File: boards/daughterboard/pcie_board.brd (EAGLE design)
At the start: 97.3 x 93 mm, 61 parts, among them IC1 XMEGA16A4A, IC2 SN754410, T1 2N3704, T2 2N3704, T3 2N3704, T4 2N3704, T5 2N3704, T6 2N3704, T7 2N3704, X1 PCI-E1X_EDGE

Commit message: Latest board(the one presented at class
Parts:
- removed ANALOG_IN, JTAG: (no value), pinhead:2X03
- removed ASYNC_INT_IN: (no value), pinhead:2X02
- removed C1, C2: (no value), capacitor-wima:C2.5-4
- removed LED_ERROR, LED_MOT_A, LED_MOT_B, LED_SELECTED: (no value), led:LED5MM
- removed MOT_A_OUT, MOT_B_OUT, TRIAC_OUT, ZEROCROSS_SENSE: (no value), pinhead:1X02
- removed PWR, PWR1, PWR2: (no value), pinhead:1X04
- removed S1: (no value), switch-dil:DA-05
- removed T1, T2, T3, T4, T5, T6, T7: 2N3704, transistor:TO92
- added CHANNEL_1_ADC, CHANNEL_2_ADC, I2C1, I2C2, JP4, JP5, JP6, OPTO_IN: (no value), pinhead:1X02
- added JP1, JP3: (no value), pinhead:2X03
- added JP10, JP11, JP12, JP13, MOTOR_1_OUT, MOTOR_2_OUT: (no value), SparkFun:SCREWTERMINAL-3.5MM-2
- added JP2, JP7, JP8, JP9, SLAVE_SELECT_2: (no value), pinhead:1X01
- added LED1, LED2, LED3: (no value), led:CHIP-LED0603
- added LED_ERROR1, LED_ERROR2, LED_MOT1, LED_MOT2: (no value), led:LED5MM
- added MPC3002ADC: (no value), ic-package:DIL08
- added OK3: TIL193, optocoupler:DIL16
- added R29, R30, R31, R32: (no value), resistor:M0805
- added SPI_OUT: (no value), pinhead:1X05
- added U$1: PCI-E1X_EDGE, con-pci_express(pci-e):PCI-E_X1_EDGE
- EXTERNAL_POWER_IN: device pinhead:1X02 -> SparkFun:SCREWTERMINAL-3.5MM-2
- OK1, OK2: value ILQ620 -> TIL193
- R1, R2, R22, R3, R5, R6, R7: value 10K -> (none); device resistor:R0805 -> resistor:M0805
- R10, R11, R15, R16, R17, R8, R9: value 47Ohm -> (none); device resistor:0207/10 -> resistor:M0805
- R12, R4: value 100Ohm -> (none); device resistor:0207/10 -> resistor:M0805
- R13, R14, R18, R19, R20: value 100Ohm -> (none); device resistor:R0805 -> resistor:M0805
- R21: value 10K -> (none); device resistor:0207/10 -> resistor:M0805
- R23, R24, R25, R26, R27, R28: value 47Ohm -> (none); device resistor:0204/7 -> resistor:M0805
- X1: value PCI-E1X_EDGE -> 9090-4R; device con-pci_express(pci-e):PCI-E_X1_EDGE -> con-thomas-betts:9090-4R
- moved R23 79.8 mm to (66.3, 23.4), turned to 0 degrees
- moved R28 79.0 mm to (72.6, -1.02)
- moved R24 71.5 mm to (66.3, 28.4), turned to 0 degrees
- moved R18 71.1 mm to (9.65, 11.9), flipped to the top
- moved R26 69.5 mm to (72.9, 31.2)
- moved R15 64.7 mm to (9.65, 33.0), turned to 0 degrees
- moved R17 64.3 mm to (9.65, 19.6), turned to 0 degrees
- moved R16 62.4 mm to (9.65, 27.2), turned to 0 degrees
- moved R1 53.7 mm to (28.7, 48.8)
- moved X1 52.4 mm to (12.7, 61.7)
- moved R3 51.3 mm to (28.7, 43.4), turned to 0 degrees
- moved R2 48.8 mm to (28.7, 53.8), turned to 0 degrees
- moved R8 48.7 mm to (49.5, -2.54), turned to 0 degrees
- moved R25 47.1 mm to (54.1, 51.6), turned to 90 degrees
- moved R4 45.3 mm to (53.6, -2.54), flipped to the top, turned to 180 degrees
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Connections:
- removed net +12V: PWR.1, PWR1.1, PWR2.1, X1.A3, X1.B3
- removed net +5V: PWR.2, PWR1.2, PWR2.2, X1.A2, X1.B2
- removed net EXT_5V: IC2.16, R1.2, R2.1, R22.2, R3.1, R5.2, R6.1, R7.1, VREG.OUT
- removed net N$15: IC1.13, R27.1
- removed net N$4: LED_POWER.A, R23.2
- removed net N$43: IC2.14, MOT_B_OUT.1
- removed net N$45: IC1.16, S1.7
- removed net N$46: IC1.15, S1.6
- removed net N$47: OK2.3, R10.1
- removed net N$48: OK2.5, R11.1
- removed net N$49: OK2.4, T2.2
- removed net N$50: OK2.6, T3.2
- removed net N$51: R12.1, T1.1
- removed net N$52: R13.1, T2.1
- removed net N$53: R14.1, T3.1
- removed net N$55: IC1.23, R14.2
- removed net N$56: IC1.24, R13.2
- removed net N$57: OK1.2, T4.2
- removed net N$58: OK1.4, T5.2
- removed net N$59: OK1.6, T6.2
- removed net N$60: R18.1, T4.1
- removed net N$61: R19.1, T5.1
- removed net N$62: R20.1, T6.1
- removed net N$65: IC1.25, R19.2
- removed net N$66: IC1.26, R20.2
- removed net N$67: OK1.1, R15.1
- removed net N$68: OK1.3, R16.1
- removed net N$69: OK1.5, R17.1
- removed net N$70: IC1.44, S1.8
- removed net N$71: ANALOG_IN.2, IC1.4
- removed net N$73: ANALOG_IN.5, IC1.40
- removed net N$74: ANALOG_IN.3, IC1.41
- removed net N$75: ASYNC_INT_IN.1, IC1.42
- removed net N$77: IC1.1, R23.1
- removed net PWM_A: IC1.21, R12.2
- removed net TRIAC_OUT: IC1.17, R4.2
- removed net ZEROCROSS_IN: IC1.27, OK2.10, R21.1
- new net ADC_CLK: MPC3002ADC.7, OK3.16, R30.1, SPI_OUT.3
- new net ADC_CS: MPC3002ADC.1, OK1.10, R27.1
- new net ADC_MISO: MPC3002ADC.6, R28.1, SPI_OUT.2
- new net ADC_MOSI: MPC3002ADC.5, OK3.14, R29.1, SPI_OUT.1
- new net ADC_VSS: CHANNEL_2_ADC.1, IC2.16, LED3.A, R19.2, R20.2, R21.1, R22.2, R23.2, R24.2, R27.2, R29.2, R30.2, R31.2, SPI_OUT.5, VREG.OUT
- new net ANALOG_1: IC1.40, JP1.1
- new net ANALOG_2: IC1.41, JP1.2
- new net ANALOG_3: IC1.43, JP1.3
- new net ANALOG_4: IC1.44, JP1.4
- new net ANALOG_5: IC1.1, JP1.5
- new net ANALOG_6: IC1.2, JP1.6
- new net ASYNC_1: IC1.22, JP8.1
- new net ASYNC_2: IC1.12, JP2.1
- new net ASYNC_3: IC1.6, JP9.1
- new net ASYNC_4: IC1.42, JP7.1
- new net CHANNEL_1: CHANNEL_1_ADC.1, MPC3002ADC.2
- new net LED_ERROR1: IC1.25, R15.2
- new net LED_ERROR2: IC1.26, R16.2
- new net LED_MOT_1: IC1.27, R17.2
- new net LED_MOT_2: IC1.33, R18.2
- new net LED_ORDERS: IC1.24, R14.2
- new net LED_POWER: IC1.23, R13.2
- new net MISO: IC1.16, OK3.12, R4.1
- new net MOSI: IC1.15, OK3.3
- new net MOT_CONTROL_A_1: IC1.13, OK1.3
- new net MOT_CONTROL_A_2: IC1.7, OK2.3
- new net MOT_CONTROL_B_1: IC1.14, OK1.5
- new net MOT_CONTROL_B_2: IC1.5, OK2.5
- new net MOT_CONTROL_EN_1: IC1.21, OK1.1
- new net MOT_CONTROL_EN_2: IC1.20, OK2.1
- new net N$38: JP10.1, JP11.1, X1.1
- new net OPTIONAL_OPTO_IN: OK3.10, R8.1
- new net PDI_CLK: IC1.35, JP3.2
- new net PDI_DATA: IC1.34, JP3.6
- new net SCK: IC1.17, OK3.1
- new net SS1: IC1.3, OK2.7
- new net SS2: IC1.4, OK1.7
- net +3V3: now also JP3.5, JP4.1, JP5.1, JP6.1, R4.2, U$1.A1, U$1.A2, U$1.B1, U$1.B2; no longer C1.1, C2.2, JTAG.2, PWR.3, PWR1.3, PWR2.3, R10.2, R11.2, R15.2, R16.2, R17.2, R21.2, R9.2, S1.1, S1.2, S1.3, S1.4, S1.5, X1.A1, X1.B1
- net ERROR: now also IC1.32, U$1.A7, U$1.B7; no longer IC1.22, X1.A6
- net EXT_MOTOR_GND: now also CHANNEL_2_ADC.2, MPC3002ADC.4, MPC3002ADC.8, OK2.9, OK3.13, OK3.15, OK3.6, R25.2, R26.2, R32.2, SPI_OUT.4; no longer TRIAC_OUT.2
- net GND: now also JP10.2, JP11.2, JP12.2, JP13.2, JP3.1, JP4.2, JP5.2, LED_ERROR1.K, LED_ERROR2.K, LED_MOT1.K, LED_MOT2.K, OK3.11, OK3.9, R1.1, R10.1, R11.1, R12.1, R2.1, R3.1, R5.1, R6.1, R7.1, R9.1, U$1.A10, U$1.A11, U$1.A12, U$1.A13, U$1.A14, U$1.A15, U$1.A16, U$1.A17, U$1.A18, U$1.A8, U$1.A9, U$1.B10, U$1.B11, U$1.B12, U$1.B13, U$1.B14, U$1.B15, U$1.B16, U$1.B17, U$1.B18, U$1.B8, U$1.B9, X1.2, X1.3; no longer C1.2, C2.1, JTAG.6, LED_ERROR.K, LED_MOT_A.K, LED_MOT_B.K, LED_SELECTED.K, OK2.9, PWR.4, PWR1.4, PWR2.4, T1.3, T2.3, T3.3, T4.3, T5.3, T6.3, T7.3, X1.A10, X1.A12, X1.A13, X1.A14, X1.A15, X1.A16, X1.A17, X1.A18, X1.A4, X1.A5, X1.A7, X1.A8, X1.B10, X1.B11, X1.B12, X1.B13, X1.B14, X1.B15, X1.B16, X1.B17, X1.B18, X1.B4, X1.B5, X1.B7, X1.B9
- net N$1: now also IC2.14, MOTOR_2_OUT.1; no longer IC1.3, R25.1
- net N$10: now also OK2.4, R6.2; no longer IC1.33, R26.1
- net N$11: now also OK2.6, R7.2; no longer LED_ERROR.A, R26.2
- net N$12: now also OK2.8, R10.2; no longer ANALOG_IN.4, IC1.5
- net N$13: now also OK3.2, R11.2; no longer ANALOG_IN.6, IC1.7
- net N$14: now also OK3.4, R12.2; no longer ASYNC_INT_IN.3, IC1.12
- net N$16: now also LED_POWER.A, R13.1; no longer ANALOG_IN.1, IC1.43
- net N$17: now also LED_ORDERS.A, R14.1; no longer IC1.14, R28.1
- net N$18: now also CHANNEL_1_ADC.2, MPC3002ADC.3; no longer ASYNC_INT_IN.4, IC1.32
- net N$19: now also OK2.10, R31.1, SLAVE_SELECT_2.1; no longer LED_MOT_B.A, R28.2
- net N$2: now also JP12.1, JP13.1, X1.4; no longer IC1.35, JTAG.5
- net N$20: now also LED_ERROR1.A, R15.1; no longer IC1.2, R24.1
- net N$21: now also LED_ERROR2.A, R16.1; no longer ASYNC_INT_IN.2, IC1.6
- net N$22: now also LED_MOT1.A, R17.1; no longer LED_MOT_A.A, R27.2
- net N$23: now also LED_MOT2.A, R18.1; no longer IC1.36, S1.9
- net N$24: now also IC2.1, LED2.A, OK1.16, R21.2; no longer IC1.37, S1.10
- net N$25: now also IC2.2, OK1.14, R19.1; no longer OK1.8, T7.2
- net N$26: now also LED2.C, R25.1; no longer JTAG.3
- net N$27: now also LED1.C, R26.1; no longer JTAG.4
- net N$28: now also IC2.9, LED1.A, OK2.16, R20.1; no longer OK2.7, ZEROCROSS_SENSE.1
- net N$29: now also IC2.7, OK1.12, R22.1; no longer OK2.2, T1.2
- net N$3: now also IC2.11, MOTOR_2_OUT.2; no longer R4.1, T7.1
- net N$30: now also IC2.15, OK2.14, R24.1; no longer OK2.1, R9.1
- net N$31: now also MOTOR_1_OUT.2; no longer MOT_A_OUT.2
- net N$32: now also MOTOR_1_OUT.1; no longer MOT_A_OUT.1
- net N$33: now also IC2.10, OK2.12, R23.1; no longer IC2.1, OK1.16, R1.1
- net N$34: now also OK3.5, R28.2; no longer IC2.2, OK1.14, R2.2
- net N$35: now also OK3.7, OPTO_IN.1; no longer IC2.7, OK1.12, R3.2
- net N$36: now also OK3.8, OPTO_IN.2; no longer OK2.8, ZEROCROSS_SENSE.2
- net N$37: now also LED3.C, R32.1; no longer IC1.20, R18.2
- net N$39: now also JP3.4; no longer IC2.11, MOT_B_OUT.2
- net N$40: now also JP3.3; no longer IC2.9, OK2.16, R5.1
- net N$41: now also IC1.36; no longer IC2.15, OK2.14, R6.2
- net N$42: now also IC1.37, JP6.2; no longer IC2.10, OK2.12, R7.2
- net N$5: now also OK1.2, R2.2; no longer OK1.10, R22.1, TRIAC_OUT.1
- net N$6: now also OK1.4, R1.2; no longer LED_ORDERS.A, R24.2
- net N$7: now also OK1.6, R3.2; no longer LED_SELECTED.A, R25.2
- net N$8: now also OK1.8, R9.2; no longer OK1.7, R8.1
- net N$9: now also OK2.2, R5.2; no longer IC1.34, JTAG.1
- net SCL1: now also I2C1.1, U$1.A3, U$1.B3; no longer X1.B6
- net SCL2: now also I2C2.1, U$1.A5, U$1.B5; no longer X1.A9
- net SDA1: now also I2C1.2, U$1.A4, U$1.B4; no longer X1.B8
- net SDA2: now also I2C2.2, U$1.A6, U$1.B6; no longer X1.A11
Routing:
- net GND: track 388.0 -> 60.6 mm, vias 3 -> 1
- net +3V3: track 381.3 -> 63.1 mm, vias 4 -> 0
- net ADC_VSS: track 0.00 -> 206.2 mm
- net SDA2: track 161.6 -> 11.6 mm, vias 1 -> 0
- net ERROR: track 140.7 -> 0.00 mm, vias 3 -> 0
- net EXT_5V: track 138.3 -> 0.00 mm, vias 2 -> 0
- net N$66: track 131.2 -> 0.00 mm, vias 2 -> 0
- net N$15: track 127.4 -> 0.00 mm
- net N$23: track 124.8 -> 0.00 mm, vias 1 -> 0
- net EXT_MOTOR_GND: track 160.7 -> 281.3 mm
- net N$17: track 103.4 -> 0.00 mm
- net SCL2: track 158.6 -> 58.8 mm
- net N$24: track 119.3 -> 24.7 mm, vias 1 -> 0
- net N$18: track 86.6 -> 5.41 mm, vias 1 -> 0
- net ADC_CS: track 0.00 -> 78.6 mm
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- removed copper zone on layer 1, net EXT_MOTOR_GND
- removed copper zone on layer 16, net EXT_MOTOR_GND
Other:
- board size 97.3 x 93 mm -> 91.2 x 77.5 mm

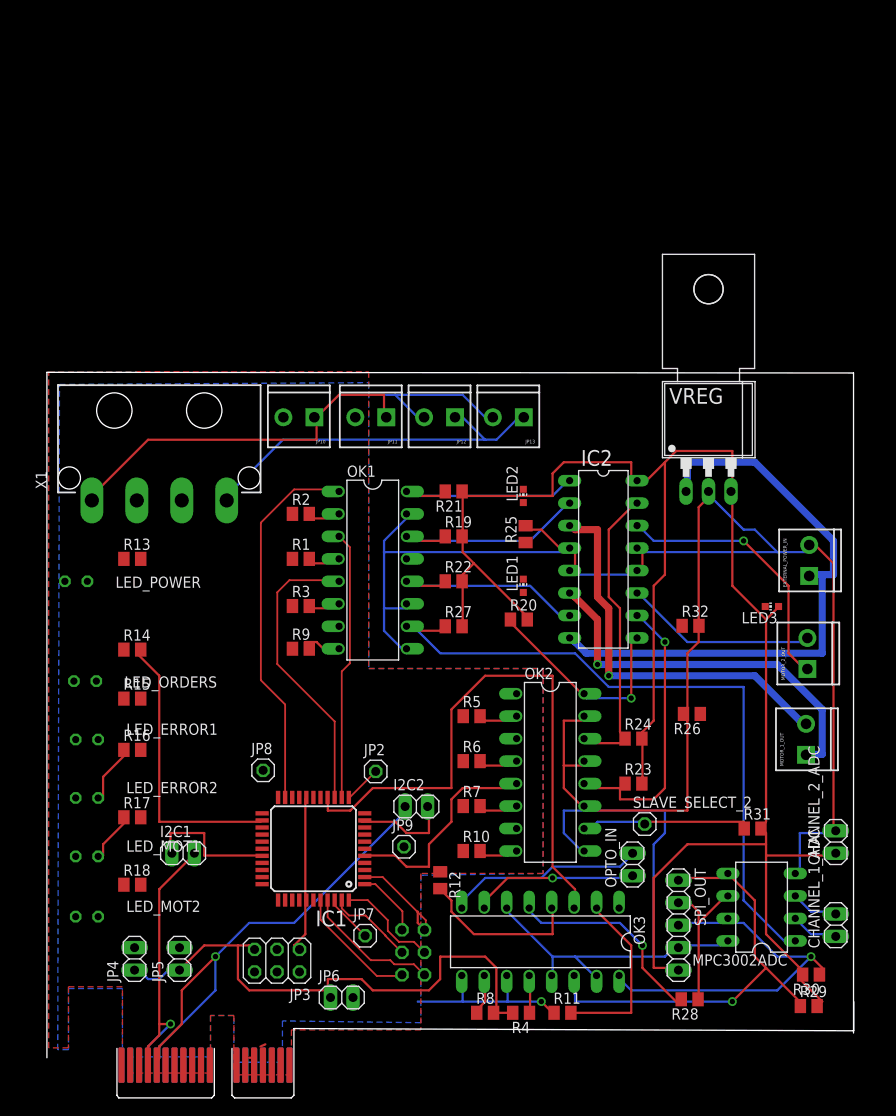
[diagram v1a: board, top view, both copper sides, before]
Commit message: added some fets to take care of the overloaded atxmega.
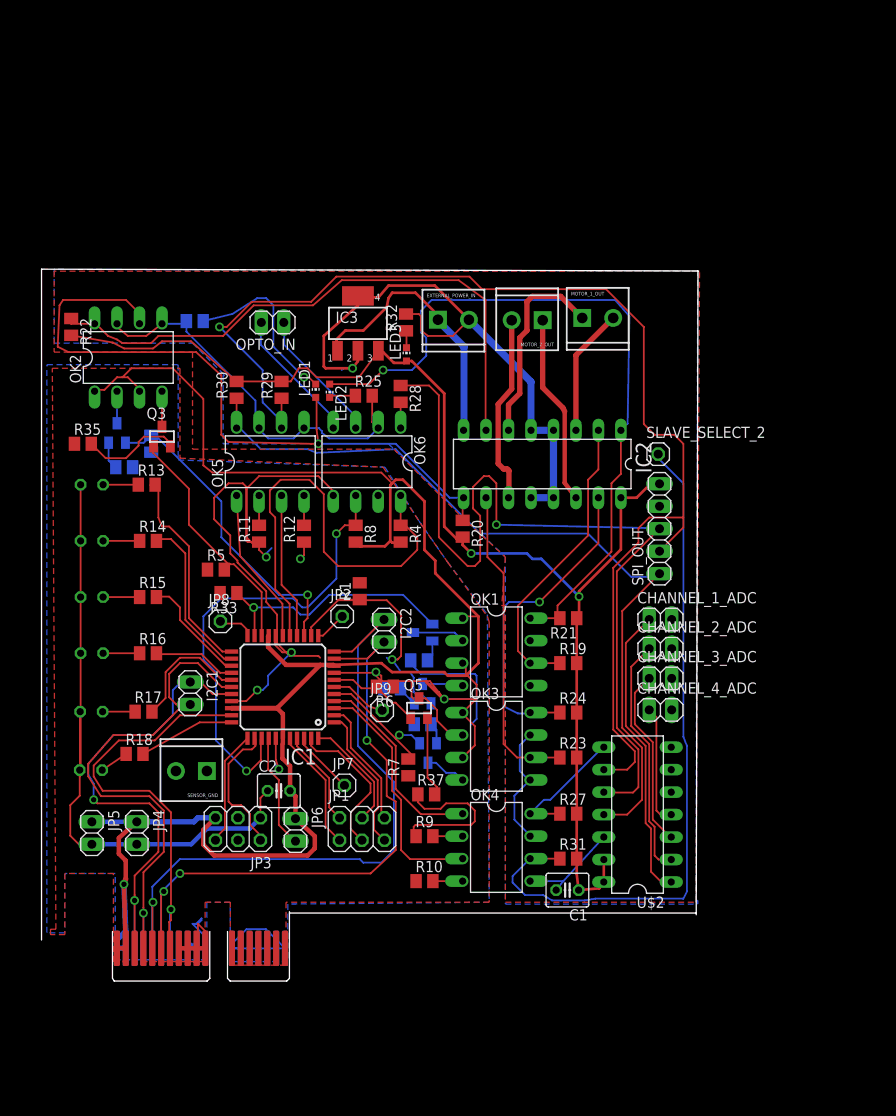
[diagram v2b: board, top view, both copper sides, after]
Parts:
- removed JP10, JP11, JP12, JP13: (no value), SparkFun:SCREWTERMINAL-3.5MM-2
- removed MPC3002ADC: (no value), ic-package:DIL08
- removed VREG: (no value), v-reg:78MXXL
- removed X1: 9090-4R, con-thomas-betts:9090-4R
- added C1, C2: (no value), resistor:C025-040X050
- added CHANNEL_3_ADC, CHANNEL_4_ADC: (no value), pinhead:1X02
- added IC3: UA78M05DCY, linear:SOT223
- added OK4, OK5, OK6: LTV826, optocoupler:DIL08
- added Q1, Q2, Q3, Q4, Q5, Q6: FDN360P, transistor-power:SUPER-SOT3
- added R33, R34, R35, R36, R37, R38: (no value), resistor:M0805
- added SENSOR_GND: (no value), SparkFun:SCREWTERMINAL-3.5MM-2
- added U$2: MCP3004, microchip:DIL14
- OK1, OK2, OK3: value TIL193 -> LTV826; device optocoupler:DIL16 -> optocoupler:DIL08
- moved R30 92.6 mm to (21.4, 67.9), turned to 90 degrees
- moved R29 91.7 mm to (26.5, 67.9), turned to 90 degrees
- moved R28 75.8 mm to (40.0, 67.4), turned to 270 degrees
- moved OPTO_IN 73.5 mm to (25.5, 75.5), turned to 180 degrees
- moved R26 71.6 mm to (16.7, 75.6), flipped to the bottom, turned to 0 degrees
- moved OK2 66.9 mm to (9.19, 71.5), turned to 0 degrees
- moved R11 64.1 mm to (24.0, 51.6), turned to 90 degrees
- moved R8 56.1 mm to (34.9, 51.6), turned to 270 degrees
- moved R4 55.8 mm to (40.0, 51.6), turned to 270 degrees
- moved MOTOR_1_OUT 55.5 mm to (60.5, 76.0), turned to 0 degrees
- moved R22 51.9 mm to (2.74, 75.0), turned to 270 degrees
- moved EXTERNAL_POWER_IN 51.0 mm to (44.2, 75.8), turned to 0 degrees
- moved LED3 50.2 mm to (40.6, 71.9), turned to 0 degrees
- moved MOTOR_2_OUT 49.5 mm to (56.0, 75.7), turned to 180 degrees
- moved R32 47.0 mm to (40.6, 75.5), turned to 90 degrees
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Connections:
- removed net ADC_VSS: CHANNEL_2_ADC.1, IC2.16, LED3.A, R19.2, R20.2, R21.1, R22.2, R23.2, R24.2, R27.2, R29.2, R30.2, R31.2, SPI_OUT.5, VREG.OUT
- removed net CHANNEL_1: CHANNEL_1_ADC.1, MPC3002ADC.2
- new net CH1: CHANNEL_1_ADC.1, U$2.1
- new net CH2: CHANNEL_2_ADC.1, U$2.2
- new net CH3: CHANNEL_3_ADC.1, U$2.3
- new net CH4: CHANNEL_4_ADC.1, U$2.4
- new net EXT_MOTOR_VCC: C1.1, IC2.16, IC3.3, LED3.A, R19.2, R20.2, R21.1, R22.2, R23.2, R24.2, R27.2, R29.2, R30.2, R31.2, SPI_OUT.5, U$2.13, U$2.14
- new net N$15: Q3.2, R35.2
- new net N$4: OK1.2, Q1.3
- net +3V3: now also C2.2, OK1.1, OK1.3, OK2.1, OK2.3, OK3.1, OK3.3
- net ADC_CLK: now also OK5.8, SPI_OUT.1, U$2.11; no longer MPC3002ADC.7, OK3.16, SPI_OUT.3
- net ADC_CS: now also OK4.8, U$2.8; no longer MPC3002ADC.1, OK1.10
- net ADC_MISO: now also SPI_OUT.3, U$2.10; no longer MPC3002ADC.6, SPI_OUT.2
- net ADC_MOSI: now also OK5.6, SPI_OUT.2, U$2.9; no longer MPC3002ADC.5, OK3.14, SPI_OUT.1
- net EXT_MOTOR_A: now also IC3.1; no longer VREG.IN
- net EXT_MOTOR_GND: now also C1.2, CHANNEL_1_ADC.2, CHANNEL_3_ADC.2, CHANNEL_4_ADC.2, IC3.2, IC3.4, OK1.5, OK1.7, OK2.5, OK2.7, OK3.5, OK3.7, OK4.5, OK4.7, OK5.5, OK5.7, OK6.2, U$2.12, U$2.7; no longer MPC3002ADC.4, MPC3002ADC.8, OK1.11, OK1.13, OK1.15, OK1.9, OK2.11, OK2.13, OK2.15, OK2.9, OK3.13, OK3.15, OK3.6, VREG.GND
- net GND: now also C2.1, OK6.5, OK6.7, R1.2, R3.2, R33.2, R34.1, R35.1, R36.1, R37.1, R38.1, SENSOR_GND.1, SENSOR_GND.2; no longer JP10.2, JP11.2, JP12.2, JP13.2, OK3.11, OK3.9, R1.1, R3.1, X1.2, X1.3
- net MISO: now also OK6.8; no longer OK3.12
- net MOSI: now also OK5.3; no longer OK3.3
- net MOT_CONTROL_A_1: now also Q2.1, R1.1; no longer OK1.3
- net MOT_CONTROL_A_2: now also Q5.1, R6.2; no longer OK2.3
- net MOT_CONTROL_B_1: now also Q4.1, R3.1; no longer OK1.5
- net MOT_CONTROL_B_2: now also Q6.1, R7.2; no longer OK2.5
- net MOT_CONTROL_EN_1: now also Q1.1, R33.1; no longer OK1.1
- net MOT_CONTROL_EN_2: now also Q3.1, R5.2; no longer OK2.1
- net N$10: now also OK3.2, Q5.3; no longer OK2.4, R6.2
- net N$11: now also Q5.2, R37.2; no longer OK2.6, R7.2
- net N$12: now also OK4.4; no longer OK2.8
- net N$13: now also OK5.2; no longer OK3.2
- net N$14: now also OK5.4; no longer OK3.4
- net N$18: now also OK2.2, Q4.3; no longer CHANNEL_1_ADC.2, MPC3002ADC.3
- net N$19: now also OK4.6; no longer OK2.10
- net N$2: now also Q1.2, R2.2; no longer JP12.1, JP13.1, X1.4
- net N$24: now also OK1.8; no longer OK1.16
- net N$25: now also OK1.6; no longer OK1.14
- net N$28: now also OK2.6; no longer OK2.16
- net N$29: now also OK2.8; no longer OK1.12
- net N$30: now also OK3.8; no longer OK2.14
- net N$33: now also OK3.6; no longer OK2.12
- net N$34: now also OK6.1; no longer OK3.5
- net N$35: now also OK6.3; no longer OK3.7
- net N$36: now also OK6.4; no longer OK3.8
- net N$38: now also Q6.2, R38.2; no longer JP10.1, JP11.1, X1.1
- net N$41: now also OK3.4, Q6.3; no longer IC1.36
- net N$5: now also Q2.2, R34.2; no longer OK1.2, R2.2
- net N$6: now also Q2.3; no longer R1.2
- net N$7: now also Q4.2, R36.2; no longer OK1.6, R3.2
- net N$8: now also OK4.2; no longer OK1.8
- net N$9: now also OK2.4, Q3.3; no longer OK2.2, R5.2
- net OPTIONAL_OPTO_IN: now also IC1.36, OK6.6; no longer OK3.10
- net SCK: now also OK5.1; no longer OK3.1
- net SS1: now also OK4.3; no longer OK2.7
- net SS2: now also OK4.1; no longer OK1.7
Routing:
- net ADC_VSS: track 206.2 -> 0.00 mm
- net GND: track 60.6 -> 248.9 mm, vias 1 -> 7
- net +3V3: track 63.1 -> 218.9 mm, vias 0 -> 1
- net EXT_MOTOR_GND: track 281.3 -> 139.2 mm, vias 0 -> 1
- net EXT_MOTOR_VCC: track 0.00 -> 141.3 mm, vias 0 -> 2
- net ADC_MOSI: track 50.3 -> 138.0 mm
- net ADC_MISO: track 17.8 -> 99.9 mm, vias 0 -> 1
- net ADC_CS: track 78.6 -> 14.8 mm
- net SDA2: track 11.6 -> 73.6 mm, vias 0 -> 3
- net N$19: track 20.4 -> 80.0 mm
- net N$24: track 24.7 -> 83.4 mm, vias 0 -> 1
- net N$28: track 26.3 -> 80.4 mm
- net ERROR: track 0.00 -> 49.7 mm, vias 0 -> 1
- net MOSI: track 65.7 -> 16.6 mm
- net ADC_CLK: track 43.7 -> 91.6 mm, vias 1 -> 0
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- added copper zone on layer 1, net EXT_MOTOR_GND
- added copper zone on layer 16, net EXT_MOTOR_GND
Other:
- board size 91.2 x 77.5 mm -> 74.2 x 75.8 mm
